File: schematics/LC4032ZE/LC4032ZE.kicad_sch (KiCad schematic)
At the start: 263 parts

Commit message: bugfixes, rebuild .sx files
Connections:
- net at U?.: now also R?.1, U?., U?.; no longer U?.
- net at U?.: now also F?.; no longer U?. (Q)
- net at U?. (Q): now also U?.; no longer U?.
- net at U?.: now also U?., U?., U?.; no longer U?.
- net at U?.: now also U?.; no longer U?. (Q) (x2)
- net at U?.: now also U?.; no longer U?. (x7)
- net at U?.: now also U?., U?.; no longer U?. (x2)
- net at U?., U?.: now also U?. (x3)
- net at U?.: now also F?., U?.; no longer U?.
- net at U?.: now also F?.; no longer U?.
- new net: R?.1, U?., U?., U?. (x4)
- new net: U?., U?. (x42)
- new net: U?., U?. (Q) (x5)
- new net: U?., U?., U?. (x9)
- new net: U?., U?., U?. (Q)
- new net: F?., U?., U?. (x7)
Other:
- note added: "90:171"
- note added: "91:171"
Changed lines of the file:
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@@
     (effects (font (size 1.27 1.27)) (justify right bottom))
   )
-  (text "89:171" (at 403.86 173.99 180)
+  (text "91:171" (at 403.86 173.99 180)
     (effects (font (size 1.27 1.27)) (justify right bottom))
   )
@@
     (effects (font (size 1.27 1.27)) (justify right bottom))
   )
-  (text "88:171" (at 403.86 161.29 180)
+  (text "90:171" (at 403.86 161.29 180)
     (effects (font (size 1.27 1.27)) (justify right bottom))
   )

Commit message: refactoring naming conventions, add osctimer to LC4032ZE schematic
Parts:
- added F? (x6): Fuse, symbol symbols:Fuse
- added U? (x2): Mux2, symbol symbols:Mux2
- added U?: divider, symbol symbols:divider
- added U?: oscillator, symbol symbols:oscillator
- added U?: Mux4, symbol symbols:Mux4
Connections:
- net Shared PT async is gone; now on net Shared PT init: U?., U?.
- net BIE_{A}: no longer U?., U?.
- net BIE_{B}: no longer U?., U?.
- net at U?.: now also R?.1, U?., U?.; no longer U?.
- net at U?.: now also F?.; no longer U?. (Q)
- net at U?. (Q): now also U?.; no longer U?.
- net at U?.: now also U?., U?., U?.; no longer U?.
- net at U?.: now also U?.; no longer U?. (Q) (x2)
- net at U?.: now also U?.; no longer U?. (x7)
- net at U?.: now also U?., U?.; no longer U?. (x2)
- net at U?., U?.: now also U?. (x3)
- net at U?.: now also F?., U?.; no longer U?.
- net at U?.: now also F?.; no longer U?.
- net Shared PT init: now reaches U?.
- net Shared PT init: no longer U?.
- new net: R?.1, U?., U?., U?. (x4)
- new net: U?., U?. (x43)
- new net: U?., U?. (Q) (x5)
- new net: U?., U?., U?. (x9)
- new net: F?., U?. (x4)
- new net: U?., U?., U?. (Q)
- new net: F?., U?., U?. (x7)
- new net: F?., U?. (Enable) (x2)
- new net: U?., U?. (Enable), U?. (Reset)
- new net: U?., U?. (Reset) (x3)
- new net A15 MC feedback to GRP: U?., U?. (Enable)
- new net B15 MC feedback to GRP: U?., U?. (Reset)
- new net Shared PT enable_{A}: U?., U?.
- new net Shared PT enable_{B}: U?., U?.
- no-connect marks 0 -> 1
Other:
- note added: "91:168"
- note added: "92:168"
- note added: "92:169"
- note added: "92:170"
- note added: "93:169"
- note added: "93:170"
- note added: "Oscillator/Timer"
- note added: "async_source"
- note added: "bclk_polarity"
- note added: "bus_maintenance"
- note added: "clock_enable_source"
- note added: "clock_source"
- note added: "cluster_routing"
- note added: "global_routing_pool"
- note added: "goe_polarity"
- note added: "init_source"
- note added: "init_state"
- note added: "input_threshold"
- note added: "invert"
- note added: "osctimer.enable"
- note added: "osctimer.osc_out"
- note added: "osctimer.timer_div"
- note added: "osctimer.timer_out"
- note added: "output_enable_source"
- note added: "output_routing"
- note added: "power_guard"
- note added: "product_terms"
- note added: "pt0_xor"
- note added: "pt4_output_enable"
- note added: "register_type"
- note added: "shared_pt_clk_polarity"
- note added: "shared_pt_init_polarity"
- note added: "shared_pt_oe_bus"
- note added: "slew_rate"
- note added: "wide_routing"
- note added: "xor"
- note added: "zero_hold_time"
- note removed: "Async init source"
- note removed: "Bus Maintenance"
- note removed: "CE Select"
- note removed: "Clock Select"
- note removed: "Decreases V_{T} when 1"
- note removed: "Fast Input register when 0"
- note removed: "Invert PT0"
- note removed: "OE Select"
- note removed: "PT0 sum enable"
- note removed: "PT2 alt. async init when 0"
- note removed: "PT4 sum enable"
- note removed: "Power Guard Disable"
- note removed: "Register type"
- note removed: "Slew rate control"
- note removed: "Swap AR/AS"
- note removed: "Wide Steering"
- note removed: "Zero hold time when 0"

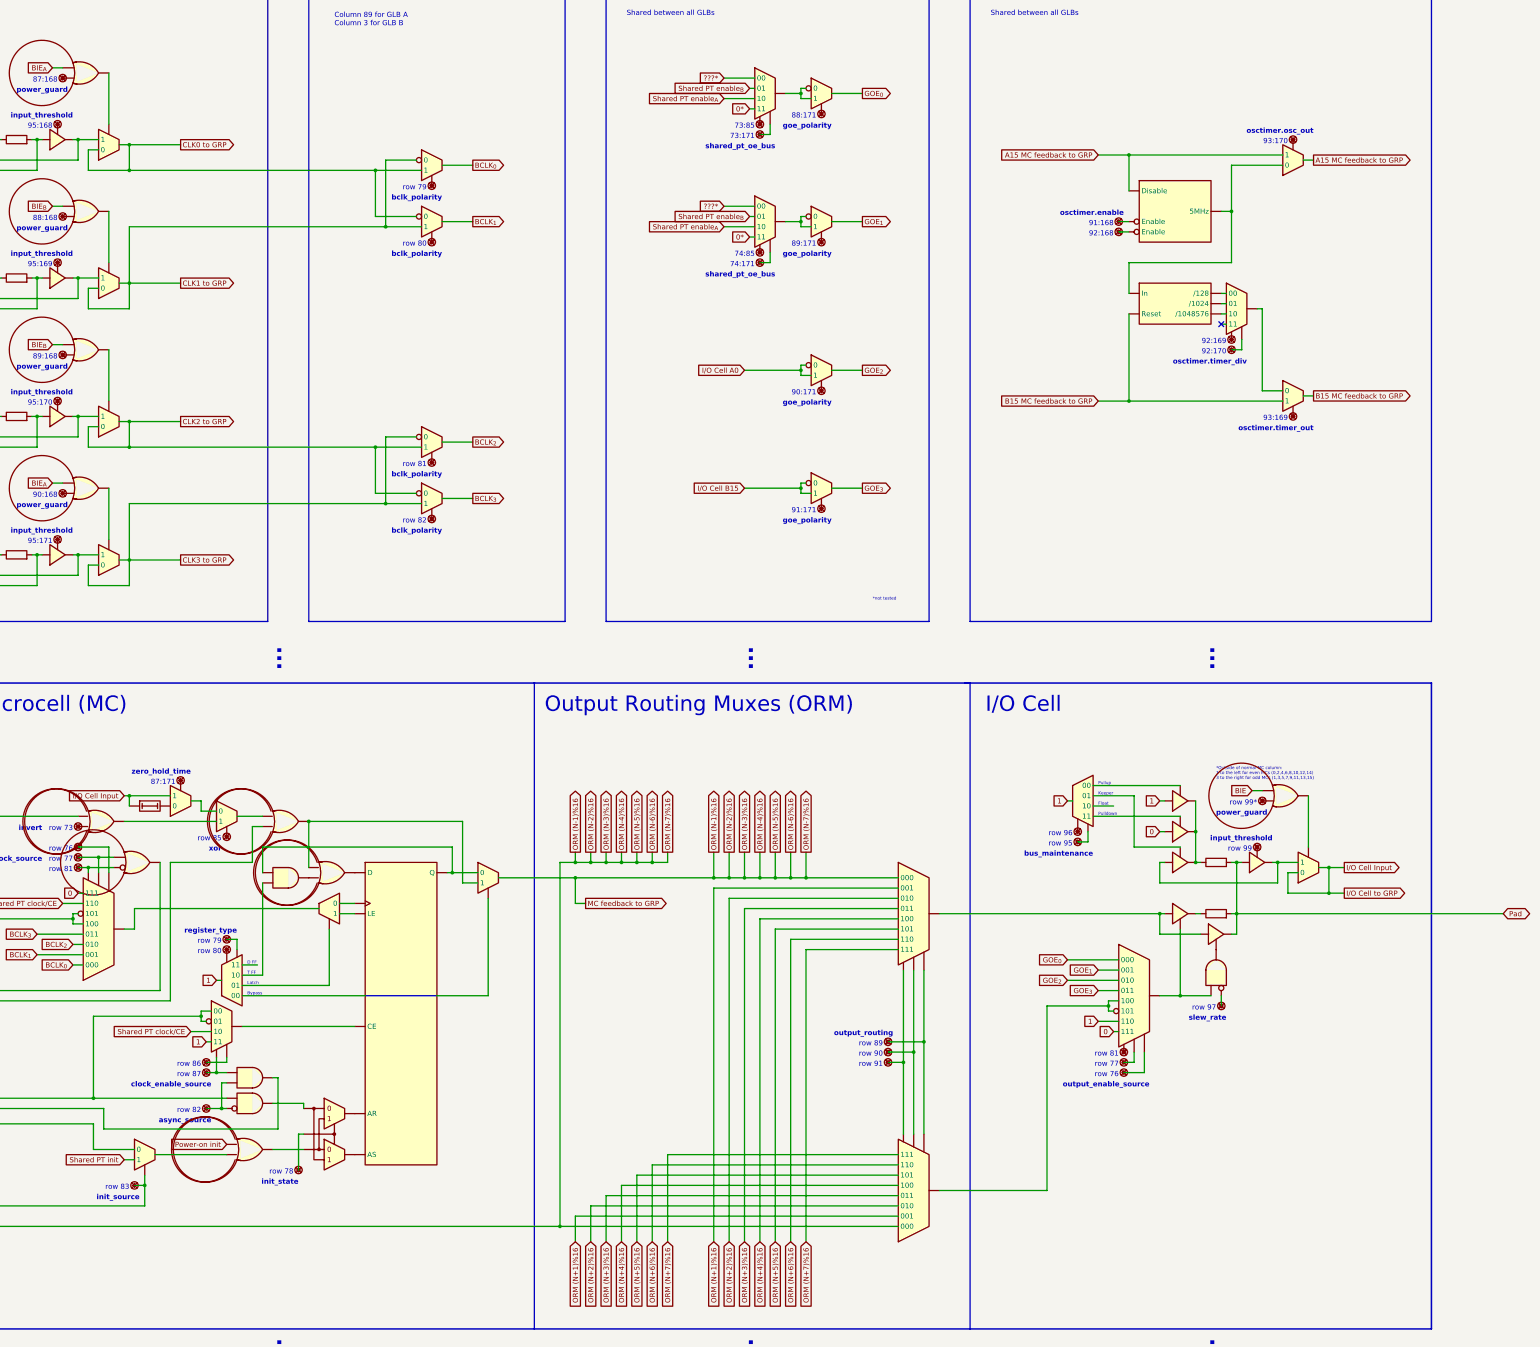
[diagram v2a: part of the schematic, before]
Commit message: Refactor to use LC4k
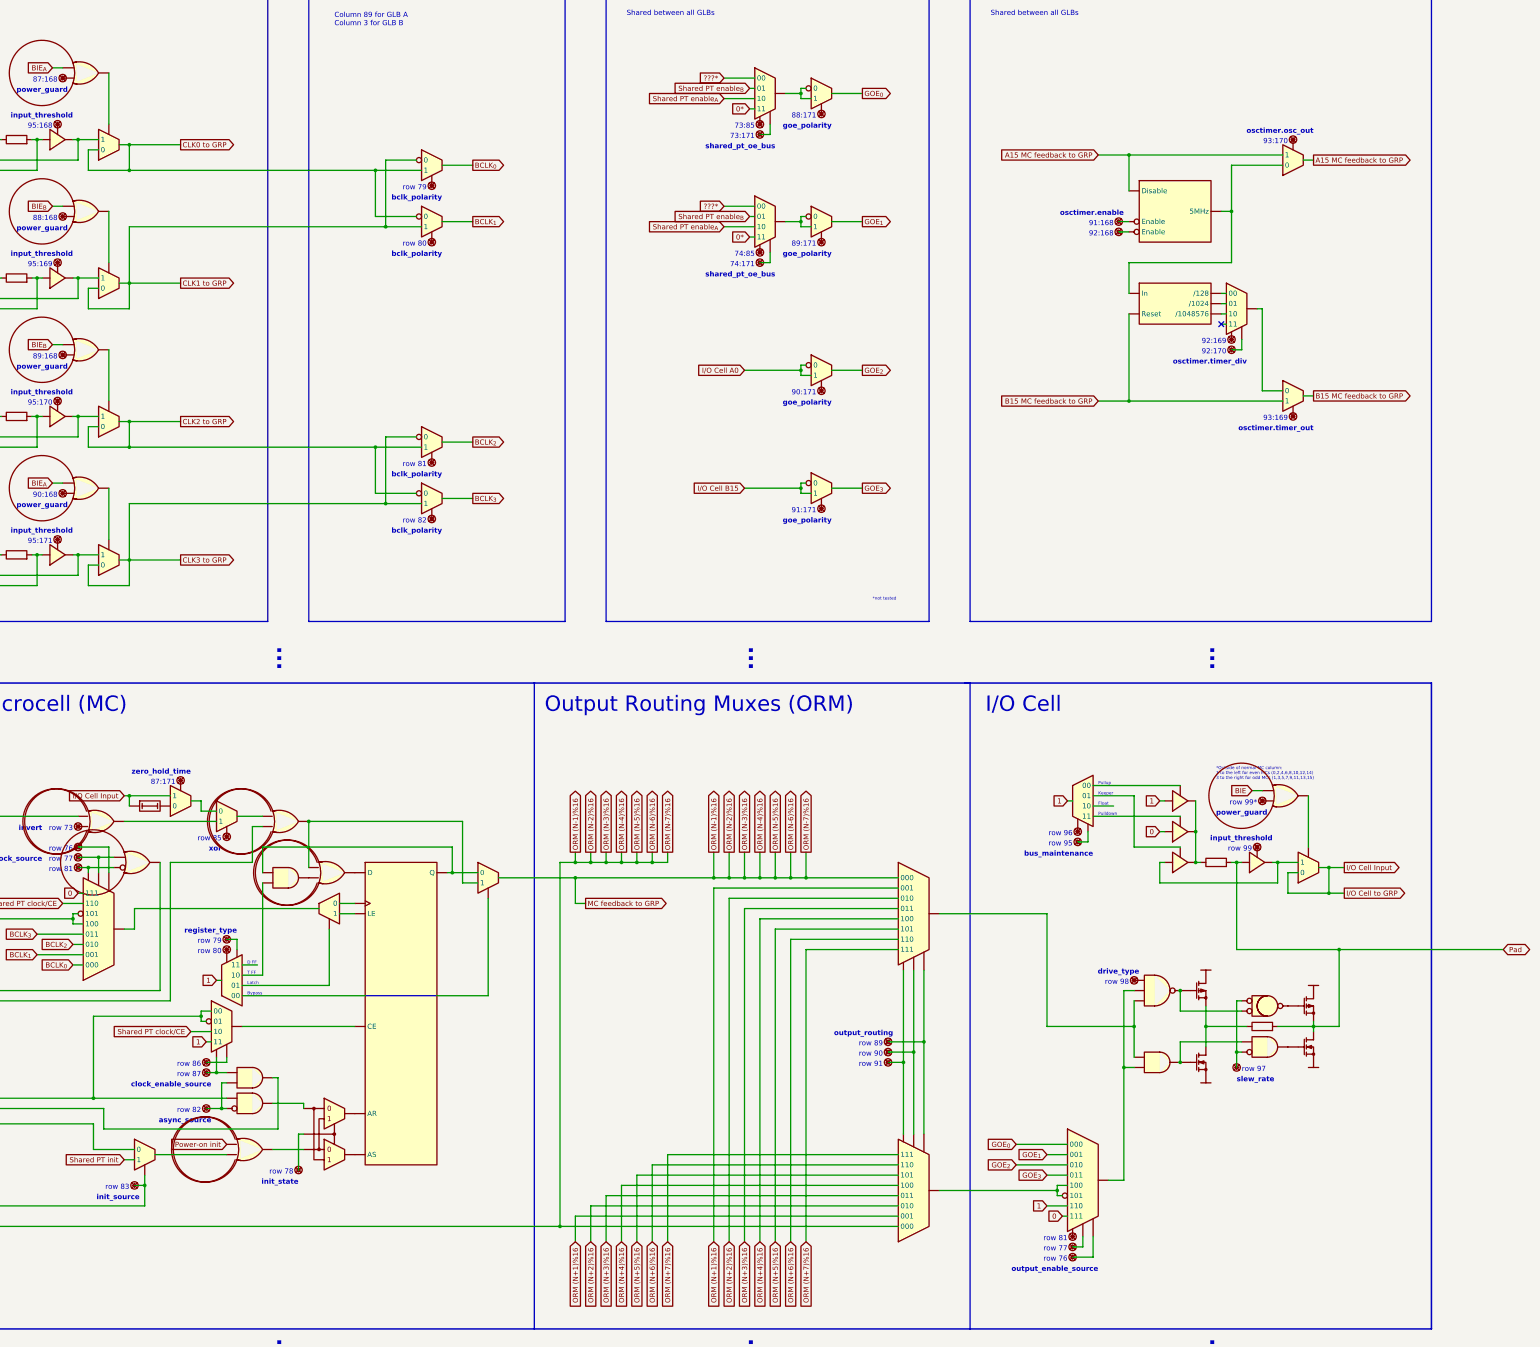
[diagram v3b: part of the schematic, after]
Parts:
- removed U? (x2): Tristate_Buffer, symbol symbols:Tristate_Buffer
- removed U?: AND2_N1, symbol symbols:AND2_N1
- added F?: Fuse, symbol symbols:Fuse
- added Q? (x2): Driver_P, symbol symbols:Driver_P
- added Q? (x2): Driver_N, symbol symbols:Driver_N
- added U?: AND2_N1, symbol symbols:AND2_N1
- added U?: OR2, symbol symbols:OR2
- added U?: NAND3, symbol symbols:NAND3
- added U?: AND2, symbol symbols:AND2
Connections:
- net Pad: now also Q?., Q?.
- net at U?.: now also R?.1, U?., U?.; no longer U?.
- net at U?.: now also F?.; no longer U?. (Q)
- net at U?. (Q): now also U?.; no longer U?.
- net at U?.: now also U?., U?., U?.; no longer U?.
- net at U?.: now also U?.; no longer U?. (Q) (x2)
- net at U?.: now also U?.; no longer U?. (x7)
- net at U?.: now also U?., U?.; no longer U?. (x2)
- net at R?.1: now also Q?., Q?.
- net at U?., U?.: now also U?. (x3)
- net at U?.: no longer U?.
- net at U?.: now also F?., U?.; no longer U?.
- net at F?.: now also U?., U?.
- net at U?.: now also F?.; no longer U?.
- new net: R?.1, U?., U?., U?. (x4)
- new net: U?., U?. (x43)
- new net: U?., U?. (Q) (x5)
- new net: U?., U?., U?. (x9)
- new net: Q?., U?., U?. (x2)
- new net: U?., U?., U?. (Q)
- new net: F?., U?., U?. (x7)
- new net: F?., U?.
- new net: Q?., U?. (x2)
- new net: U?., U?. (Enable), U?. (Reset)
- new net: U?., U?. (Reset) (x3)
- now unconnected: U?., U?., U?.
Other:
- note added: "drive_type"
- note added: "row 98"
